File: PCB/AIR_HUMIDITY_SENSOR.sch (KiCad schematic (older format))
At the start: 2 parts, among them U11 HIH712x

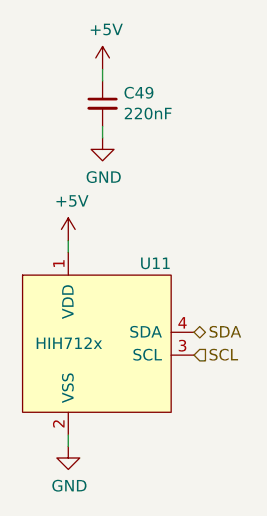
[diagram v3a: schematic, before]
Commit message: Added remaining test points
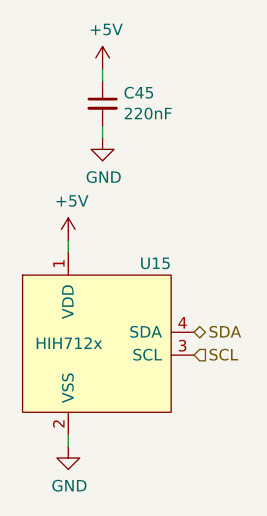
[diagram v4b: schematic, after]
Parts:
- renumbered C49 to C45, U11 to U15
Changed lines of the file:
@@
 $EndDescr
 $Comp
-L custom:HIH712x U11
+L custom:HIH712x U15
 U 1 1 5E9303FE
 P 5800 3900
-F 0 "U11" H 6250 4250 50  0000 R CNN
+F 0 "U15" H 6250 4250 50  0000 R CNN
 F 1 "HIH712x" H 5950 3900 50  0000 R CNN
 F 2 "" H 5800 3900 50  0001 C CNN
@@
 $EndComp
 $Comp
-L Device:C_Small C49
+L Device:C_Small C45
 U 1 1 5E931061
 P 5950 2850
-F 0 "C49" H 6042 2896 50  0000 L CNN
+F 0 "C45" H 6042 2896 50  0000 L CNN
 F 1 "220nF" H 6042 2805 50  0000 L CNN
 F 2 "" H 5950 2850 50  0001 C CNN
@@
 $EndComp
 $Comp
-L power:+5V #PWR0159
+L power:+5V #PWR0145
 U 1 1 5E93133D
 P 5950 2700
-F 0 "#PWR0159" H 5950 2550 50  0001 C CNN
+F 0 "#PWR0145" H 5950 2550 50  0001 C CNN
 F 1 "+5V" H 5965 2873 50  0000 C CNN
 F 2 "" H 5950 2700 50  0001 C CNN
@@
 $EndComp
 $Comp
-L power:GND #PWR0158
+L power:GND #PWR0144
 U 1 1 5E93145F
 P 5800 4350
-F 0 "#PWR0158" H 5800 4100 50  0001 C CNN
+F 0 "#PWR0144" H 5800 4100 50  0001 C CNN
 F 1 "GND" H 5805 4177 50  0000 C CNN
 F 2 "" H 5800 4350 50  0001 C CNN
@@
 $EndComp
 $Comp
-L power:+5V #PWR0157
+L power:+5V #PWR0143
 U 1 1 5E93181D
 P 5800 3450
-F 0 "#PWR0157" H 5800 3300 50  0001 C CNN
+F 0 "#PWR0143" H 5800 3300 50  0001 C CNN
 F 1 "+5V" H 5815 3623 50  0000 C CNN
 F 2 "" H 5800 3450 50  0001 C CNN
@@
 $EndComp
 $Comp
-L power:GND #PWR0160
+L power:GND #PWR0146
 U 1 1 5E931D8D
 P 5950 3000
-F 0 "#PWR0160" H 5950 2750 50  0001 C CNN
+F 0 "#PWR0146" H 5950 2750 50  0001 C CNN
 F 1 "GND" H 5955 2827 50  0000 C CNN
 F 2 "" H 5950 3000 50  0001 C CNN

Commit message: Added majority footprints
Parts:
- C45: footprint (none) -> Capacitor_SMD:C_0603_1608Metric
- U15: footprint (none) -> Connector_PinHeader_1.27mm:PinHeader_1x04_P1.27mm_Vertical
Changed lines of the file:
@@
 F 0 "U15" H 6250 4250 50  0000 R CNN
 F 1 "HIH712x" H 5950 3900 50  0000 R CNN
-F 2 "" H 5800 3900 50  0001 C CNN
+F 2 "Connector_PinHeader_1.27mm:PinHeader_1x04_P1.27mm_Vertical" H 5800 3900 50  0001 C CNN
 F 3 "https://sensing.honeywell.com/index.php?ci_id=147071" H 5800 3900 50  0001 C CNN
 	1    5800 3900
@@
 F 0 "C45" H 6042 2896 50  0000 L CNN
 F 1 "220nF" H 6042 2805 50  0000 L CNN
-F 2 "" H 5950 2850 50  0001 C CNN
+F 2 "Capacitor_SMD:C_0603_1608Metric" H 5950 2850 50  0001 C CNN
 F 3 "~" H 5950 2850 50  0001 C CNN
 F 4 "X7R" H 5950 2850 50  0001 C CNN "Dielectric"
